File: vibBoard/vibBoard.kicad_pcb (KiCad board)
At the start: 2 copper layers, 32.4 x 45.1 mm, 39 parts, among them J1 CAN Bus Connector, J2 Programming Header, J3 Micro_SD_Card, U1 SPX3819M5-L-3-3, U2 INA180, U3 AIS3624DQTR, U4 PIC18F26K83, U5 MCP2562, Y1 12MHz Crystal

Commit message: updated date
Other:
- board text added: "Vibration Board V1 Ishman Mann 2024-02-01"
- board text removed: "Vibration Board V1 Ishman Mann 2024-01-13"
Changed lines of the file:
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@@
     (effects (font (size 1.5 1.5) (thickness 0.3) bold) (justify left bottom))
   )
-  (gr_text "Vibration Board V1\nIshman Mann\n2024-01-13" (at 125.984 110.236) (layer "F.SilkS")
+  (gr_text "Vibration Board V1\nIshman Mann\n2024-02-01" (at 125.984 110.236) (layer "F.SilkS")
     (effects (font (size 0.8001 0.635) (thickness 0.127) bold))
   )

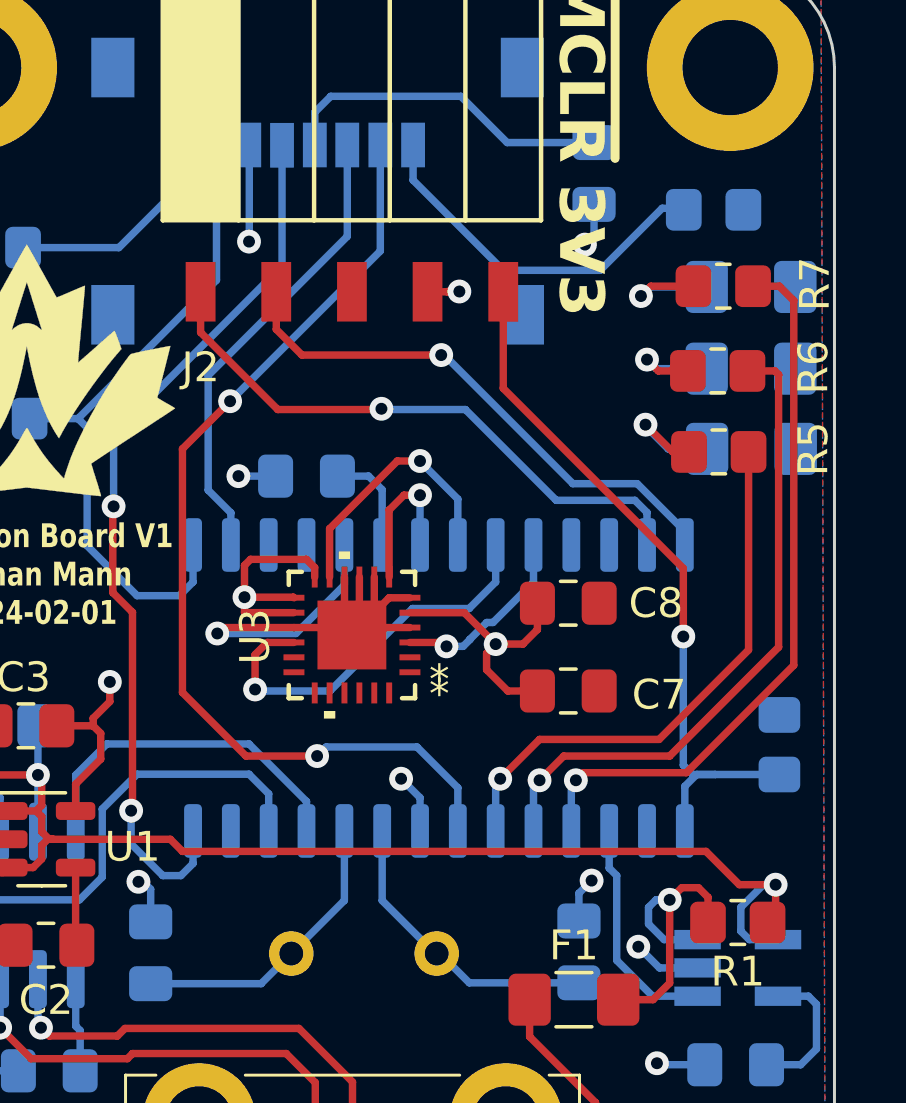
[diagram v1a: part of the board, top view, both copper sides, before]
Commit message: switched diode side and added more continuity to planes
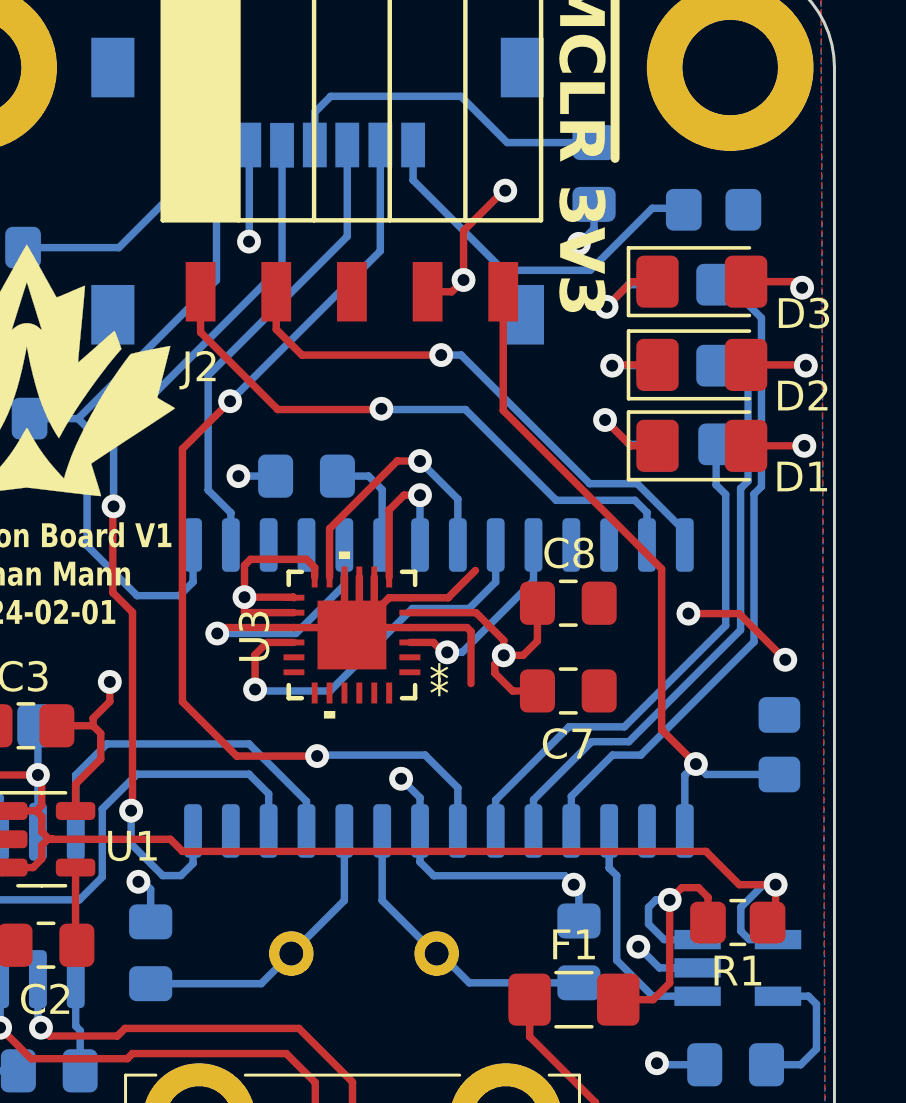
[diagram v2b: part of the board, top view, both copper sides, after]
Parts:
- D1, D2, D3: moved to F.Cu
- R5, R6, R7: moved to B.Cu
- moved D1 1.67 mm to (148.4, 105.9)
- moved D3 1.66 mm to (148.4, 100.4)
- moved D2 1.66 mm to (148.4, 103.2)
- moved R7 1.31 mm to (147.8, 100.5)
- moved R6 1.13 mm to (147.8, 103.2)
- moved R5 1.12 mm to (147.9, 105.9)
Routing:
- net +3.3V: track 47.8 -> 62.1 mm, vias 4 -> 10
- net GND: track 52.1 -> 65.3 mm
- net Net-(U4-RA2): track 24.7 -> 22.0 mm, vias 1 -> 0
- net Net-(U4-RA3): track 22.0 -> 19.7 mm, vias 1 -> 0
- net Net-(U4-RA4): track 18.7 -> 17.4 mm, vias 1 -> 0
- net Net-(D2-K): track 3.75 -> 2.95 mm
- net /~{MCLR}: track 24.5 -> 23.9 mm

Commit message: touch up
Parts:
- moved Y1 0.45 mm to (139.5, 123.4)
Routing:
- net /CANL: track 14.4 -> 13.5 mm
- net /CANH: track 19.1 -> 18.6 mm
- net GND: vias 13 -> 32
- added copper zone on B.Cu, net GND
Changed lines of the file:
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@@
   )
   (footprint "Crystal:Crystal_HC49-4H_Vertical" (layer "B.Cu")
-    (at 139.4968 122.962 180)
+    (at 139.5468 123.412 180)
     (descr "Crystal THT HC-49-4H http://5hertz.com/pdfs/04404_D.pdf")
     (tags "THT crystalHC-49-4H")
@@
   (segment (start 132.33 112.018) (end 134.7057 112.018) (width 0.25) (layer "F.Cu") (net 2))
   (segment (start 136.902 112.018) (end 136.652 112.268) (width 0.25) (layer "F.Cu") (net 2))
+  (via (at 140.65 122.05) (size 0.8) (drill 0.4) (layers "F.Cu" "B.Cu") (free) (net 2))
+  (via (at 139.25 125.25) (size 0.8) (drill 0.4) (layers "F.Cu" "B.Cu") (free) (net 2))
   (via (at 129.484901 120.552699) (size 0.8) (drill 0.4) (layers "F.Cu" "B.Cu") (net 2))
   (via (at 132.1308 112.2172) (size 0.8) (drill 0.4) (layers "F.Cu" "B.Cu") (net 2))
   (via (at 133.1976 99.06) (size 0.8) (drill 0.4) (layers "F.Cu" "B.Cu") (net 2))
   (via (at 123.2662 126.9238) (size 0.8) (drill 0.4) (layers "F.Cu" "B.Cu") (net 2))
+  (via (at 132.55 121.3) (size 0.8) (drill 0.4) (layers "F.Cu" "B.Cu") (free) (net 2))
+  (via (at 138.25 124.6) (size 0.8) (drill 0.4) (layers "F.Cu" "B.Cu") (free) (net 2))
+  (via (at 133.5 122.05) (size 0.8) (drill 0.4) (layers "F.Cu" "B.Cu") (free) (net 2))
+  (via (at 133.8 125.0255) (size 0.8) (drill 0.4) (layers "F.Cu" "B.Cu") (free) (net 2))
+  (via (at 140.4 125) (size 0.8) (drill 0.4) (layers "F.Cu" "B.Cu") (free) (net 2))
+  (via (at 135.95 124.6) (size 0.8) (drill 0.4) (layers "F.Cu" "B.Cu") (free) (net 2))
   (via (at 121.666 125.7554) (size 0.8) (drill 0.4) (layers "F.Cu" "B.Cu") (net 2))
+  (via (at 134.5 121.6) (size 0.8) (drill 0.4) (layers "F.Cu" "B.Cu") (free) (net 2))
   (via (at 146.2665 122.7328) (size 0.8) (drill 0.4) (layers "F.Cu" "B.Cu") (net 2))
+  (via (at 132.85 122.85) (size 0.8) (drill 0.4) (layers "F.Cu" "B.Cu") (free) (net 2))
+  (via (at 141.6 121.25) (size 0.8) (drill 0.4) (layers "F.Cu" "B.Cu") (free) (net 2))
+  (via (at 137.85 123.6) (size 0.8) (drill 0.4) (layers "F.Cu" "B.Cu") (free) (net 2))
+  (via (at 139.5 121.6) (size 0.8) (drill 0.4) (layers "F.Cu" "B.Cu") (free) (net 2))
   (via (at 146.8921 126.6444) (size 0.8) (drill 0.4) (layers "F.Cu" "B.Cu") (net 2))
   (via (at 144.272 99.1362) (size 0.8) (drill 0.4) (layers "F.Cu" "B.Cu") (net 2))
+  (via (at 141.25 125) (size 0.8) (drill 0.4) (layers "F.Cu" "B.Cu") (free) (net 2))
+  (via (at 135.05 125.2) (size 0.8) (drill 0.4) (layers "F.Cu" "B.Cu") (free) (net 2))
   (via (at 132.842 106.934) (size 0.8) (drill 0.4) (layers "F.Cu" "B.Cu") (net 2))
   (via (at 138.303 117.094) (size 0.8) (drill 0.4) (layers "F.Cu" "B.Cu") (net 2))
+  (via (at 132.95 125.0255) (size 0.8) (drill 0.4) (layers "F.Cu" "B.Cu") (free) (net 2))
   (via (at 122.555 116.205) (size 0.8) (drill 0.4) (layers "F.Cu" "B.Cu") (net 2))
+  (via (at 136.35 123.6) (size 0.8) (drill 0.4) (layers "F.Cu" "B.Cu") (free) (net 2))
+  (via (at 137.1 122.6) (size 0.8) (drill 0.4) (layers "F.Cu" "B.Cu") (free) (net 2))
   (via (at 135.6868 131.4704) (size 0.8) (drill 0.4) (layers "F.Cu" "B.Cu") (net 2))
   (via (at 144.1 120.65) (size 0.8) (drill 0.4) (layers "F.Cu" "B.Cu") (net 2))
+  (via (at 141.3 122.85) (size 0.8) (drill 0.4) (layers "F.Cu" "B.Cu") (free) (net 2))
   (segment (start 122.555 116.713) (end 123.0376 117.1956) (width 0.25) (layer "B.Cu") (net 2))
   (segment (start 144.78 98.6282) (end 144.272 99.1362) (width 0.25) (layer "B.Cu") (net 2))
@@
   (segment (start 152.2476 124.6632) (end 152.2476 126.1657) (width 0.25) (layer "B.Cu") (net 4))
   (segment (start 137.2108 106.934) (end 137.668 107.3912) (width 0.25) (layer "B.Cu") (net 4))
-  (segment (start 137.668 121.1834) (end 139.4466 122.962) (width 0.25) (layer "B.Cu") (net 5))
-  (segment (start 137.668 118.846) (end 137.668 121.1834) (width 0.25) (layer "B.Cu") (net 5))
-  (segment (start 144.272 123.9442) (end 140.5922 123.9442) (width 0.25) (layer "B.Cu") (net 5))
+  (segment (start 144.272 123.9442) (end 140.079 123.9442) (width 0.25) (layer "B.Cu") (net 5))
+  (segment (start 140.079 123.9442) (end 139.5468 123.412) (width 0.25) (layer "B.Cu") (net 5))
+  (segment (start 137.668 121.5332) (end 139.5468 123.412) (width 0.25) (layer "B.Cu") (net 5))
   (segment (start 139.3196 122.962) (end 139.61 122.962) (width 0.25) (layer "B.Cu") (net 5))
   (segment (start 139.4466 122.962) (end 139.4968 122.962) (width 0.25) (layer "B.Cu") (net 5))
-  (segment (start 140.5922 123.9442) (end 139.61 122.962) (width 0.25) (layer "B.Cu") (net 5))
+  (segment (start 137.668 118.846) (end 137.668 121.5332) (width 0.25) (layer "B.Cu") (net 5))
+  (segment (start 136.398 118.846) (end 136.398 121.6808) (width 0.25) (layer "B.Cu") (net 6))
+  (segment (start 136.398 121.6808) (end 134.6668 123.412) (width 0.25) (layer "B.Cu") (net 6))
   (segment (start 134.7464 122.962) (end 134.73 122.962) (width 0.25) (layer "B.Cu") (net 6))
-  (segment (start 136.398 118.846) (end 136.398 121.1808) (width 0.25) (layer "B.Cu") (net 6))
-  (segment (start 129.8956 123.9735) (end 133.6053 123.9735) (width 0.25) (layer "B.Cu") (net 6))
-  (segment (start 133.6053 123.9735) (end 134.6168 122.962) (width 0.25) (layer "B.Cu") (net 6))
-  (segment (start 136.398 121.1808) (end 134.6168 122.962) (width 0.25) (layer "B.Cu") (net 6))
+  (segment (start 129.8956 123.9735) (end 134.1053 123.9735) (width 0.25) (layer "B.Cu") (net 6))
+  (segment (start 134.1053 123.9735) (end 134.6668 123.412) (width 0.25) (layer "B.Cu") (net 6))
   (segment (start 145.15 105.05) (end 146.018 105.918) (width 0.25) (layer "F.Cu") (net 7))
   (segment (start 146.018 105.918) (end 146.9104 105.918) (width 0.25) (layer "F.Cu") (net 7))
@@
   (segment (start 147.132 122.494) (end 148.256 122.494) (width 0.25) (layer "B.Cu") (net 11))
   (segment (start 146.8628 121.158) (end 146.6088 121.412) (width 0.25) (layer "B.Cu") (net 11))
-  (segment (start 126.492 125.73) (end 128.778 125.73) (width 0.25) (layer "F.Cu") (net 13))
-  (segment (start 128.778 125.73) (end 129.032 125.476) (width 0.25) (layer "F.Cu") (net 13))
-  (segment (start 126.2126 125.4506) (end 126.492 125.73) (width 0.25) (layer "F.Cu") (net 13))
-  (segment (start 136.672 127.274) (end 136.672 128.544) (width 0.25) (layer "F.Cu") (net 13))
-  (segment (start 129.032 125.476) (end 134.874 125.476) (width 0.25) (layer "F.Cu") (net 13))
-  (segment (start 134.874 125.476) (end 136.672 127.274) (width 0.25) (layer "F.Cu") (net 13))
+  (segment (start 126.2126 125.4506) (end 126.712 125.95) (width 0.25) (layer "F.Cu") (net 13))
+  (segment (start 130.313604 125.8) (end 133.928 125.8) (width 0.25) (layer "F.Cu") (net 13))
+  (segment (start 133.928 125.8) (end 136.672 128.544) (width 0.25) (layer "F.Cu") (net 13))
+  (segment (start 130.163604 125.95) (end 130.313604 125.8) (width 0.25) (layer "F.Cu") (net 13))
+  (segment (start 126.712 125.95) (end 130.163604 125.95) (width 0.25) (layer "F.Cu") (net 13))
   (via (at 126.2126 125.4506) (size 0.8) (drill 0.4) (layers "F.Cu" "B.Cu") (net 13))
   (segment (start 126.2126 125.4506) (end 126.111 125.349) (width 0.25) (layer "B.Cu") (net 13))
   (segment (start 126.111 125.349) (end 126.111 123.822) (width 0.25) (layer "B.Cu") (net 13))
-  (segment (start 135.422 127.294) (end 135.422 128.544) (width 0.25) (layer "F.Cu") (net 14))
-  (segment (start 129.113 126.492) (end 129.286 126.319) (width 0.25) (layer "F.Cu") (net 14))
-  (segment (start 134.447 126.319) (end 135.422 127.294) (width 0.25) (layer "F.Cu") (net 14))
+  (segment (start 130.258 126.492) (end 130.5 126.25) (width 0.25) (layer "F.Cu") (net 14))
+  (segment (start 133.4 126.25) (end 135.422 128.272) (width 0.25) (layer "F.Cu") (net 14))
+  (segment (start 130.5 126.25) (end 133.4 126.25) (width 0.25) (layer "F.Cu") (net 14))
+  (segment (start 135.422 128.272) (end 135.422 128.544) (width 0.25) (layer "F.Cu") (net 14))
   (segment (start 124.841 125.4506) (end 125.8824 126.492) (width 0.25) (layer "F.Cu") (net 14))
-  (segment (start 129.286 126.319) (end 134.447 126.319) (width 0.25) (layer "F.Cu") (net 14))
-  (segment (start 125.8824 126.492) (end 129.113 126.492) (width 0.25) (layer "F.Cu") (net 14))
+  (segment (start 125.8824 126.492) (end 130.258 126.492) (width 0.25) (layer "F.Cu") (net 14))
   (via (at 124.841 125.4506) (size 0.8) (drill 0.4) (layers "F.Cu" "B.Cu") (net 14))
   (segment (start 135.2604 128.544) (end 133.7564 130.048) (width 0.25) (layer "B.Cu") (net 14))
@@
     (polygon
       (pts
-        (xy 120.9548 90.0684)
-        (xy 120.8786 134.3152)
-        (xy 152.5524 134.3152)
-        (xy 152.4 90.1446)
+        (xy 120.15 89.25)
+        (xy 119.8 135.7)
+        (xy 153.6 135.75)
+        (xy 153.4 89.3)
       )
     )
@@
     (polygon
       (pts
-        (xy 120.9294 90.0684)
-        (xy 120.8786 134.3152)
-        (xy 152.5524 134.366)
-        (xy 152.4 90.1446)
+        (xy 120.1 89.3)
+        (xy 119.8 135.7)
+        (xy 153.6 135.75)
+        (xy 153.35 89.3)
       )
     )
+  )
+  (zone (net 2) (net_name "GND") (layer "B.Cu") (hatch edge 0.5)
+    (priority 5)
+    (connect_pads (clearance 0.5))
+    (min_thickness 0.25) (filled_areas_thickness no)
+    (fill yes (thermal_gap 0.5) (thermal_bridge_width 0.5))
+    (polygon
+      (pts
+        (xy 132.1 120.8)
+        (xy 132.1 125.8)
+        (xy 142.05 125.75)
+        (xy 142.05 120.8)
+      )
+    )

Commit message: layout
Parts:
- added J4: THMS Connector, Connector_JST:JST_PH_S2B-PH-K_1x02_P2.00mm_Horizontal, F.Cu at (165.4, 126.0)
- added J5: PT 1 Connector, Connector_JST:JST_PH_S3B-PH-K_1x03_P2.00mm_Horizontal, F.Cu at (165.4, 118.9)
- added J6: PT 2 Connector, Connector_JST:JST_PH_S3B-PH-K_1x03_P2.00mm_Horizontal, F.Cu at (165.4, 109.5)
- added R10: 5kR, Resistor_SMD:R_0805_2012Metric_Pad1.20x1.40mm_HandSolder, B.Cu at (160.5, 113.5)
- added R11: 10kR, Resistor_SMD:R_0805_2012Metric_Pad1.20x1.40mm_HandSolder, B.Cu at (160.5, 108.4)
- added R12: 5kR, Resistor_SMD:R_0805_2012Metric_Pad1.20x1.40mm_HandSolder, B.Cu at (156.5, 103.9)
- added R13: 10kR, Resistor_SMD:R_0805_2012Metric_Pad1.20x1.40mm_HandSolder, B.Cu at (156.5, 99.1)
- added R9: 10kR, Resistor_SMD:R_0805_2012Metric_Pad1.20x1.40mm_HandSolder, B.Cu at (147.3, 127.8)
- C1, C2, C3, F1, R1, U1: moved to B.Cu
- C10, C12, C5, C6, C9, J3, TP1, U5, Y1: moved to F.Cu
- moved C1 38.8 mm to (160.8, 125.0), turned to 90 degrees
- moved C12 33.4 mm to (158.2, 118.4), turned to 180 degrees
- moved U5 32.2 mm to (157.6, 123.8)
- moved U1 32.0 mm to (157.5, 125.6), turned to 90 degrees
- moved C10 31.6 mm to (158.0, 129.5), turned to 180 degrees
- moved C2 27.9 mm to (154.2, 125.5), turned to -90 degrees
- moved D1 27.3 mm to (133.4, 128.7), turned to 180 degrees
- moved R5 27.1 mm to (133.3, 128.7)
- moved D2 26.9 mm to (133.4, 125.5), turned to 180 degrees
- moved C3 26.6 mm to (150.9, 124.0), turned to 90 degrees
- moved R6 26.6 mm to (133.3, 125.6), turned to 180 degrees
- moved D3 26.6 mm to (133.4, 122.3), turned to 180 degrees
- moved R7 26.1 mm to (133.3, 122.3), turned to 180 degrees
- moved C9 25.7 mm to (132.6, 119.4), turned to 0 degrees
- moved G*** 24.6 mm to (101.1, 102.6)
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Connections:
- net /PIC_CANRX renamed /CANRX
- net /PIC_CANTX renamed /CANTX
- net /PIC_SCK1 renamed /MICRO_SD_SCK
- net /PIC_SDI1 renamed /MICRO_SD_SDI
- net /PIC_SDO1 renamed /MICRO_SD_SDO
- U4 pad 2: unconnected-(U4-RA0-Pad2) -> /THMS_SENSE
- U4 pad 25: unconnected-(U4-RB4-Pad25) -> /PT_2_SENSE
- U4 pad 26: unconnected-(U4-RB5-Pad26) -> /PT_1_SENSE
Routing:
- net GND: track 65.3 -> 0.00 mm, vias 32 -> 0
- net +3.3V: track 62.1 -> 0.00 mm, vias 10 -> 0
- net +5V: track 45.2 -> 0.00 mm, vias 2 -> 0
- net /MICRO_SD_CS: track 33.4 -> 0.00 mm, vias 2 -> 0
- net /MICRO_SD_SCK: track 29.9 -> 0.00 mm, vias 2 -> 0
- net /~{MCLR}: track 23.9 -> 0.00 mm, vias 1 -> 0
- net /MICRO_SD_SDI: track 23.2 -> 0.00 mm
- net Net-(U4-RA2): track 22.0 -> 0.00 mm
- net /ICSPCLK: track 20.0 -> 0.00 mm, vias 1 -> 0
- net Net-(U4-RA3): track 19.7 -> 0.00 mm
- net /CANH: track 18.6 -> 0.00 mm, vias 1 -> 0
- net /ICSPDAT: track 18.2 -> 0.00 mm, vias 1 -> 0
- net Net-(U4-RA4): track 17.4 -> 0.00 mm
- net /CANRX: track 16.8 -> 0.00 mm
- net Net-(J1-Pin_5): track 16.6 -> 0.00 mm
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- removed copper zone on B.Cu, net +3.3V
- removed copper zone on B.Cu, net GND
- removed copper zone on F.Cu, net GND
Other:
- board size 32.4 x 45.1 mm -> 45.7 x 45.7 mm
- board text added: "Vibration Board V2 Ishman Mann 2024-03-14"
- board text removed: "Vibration Board V1 Ishman Mann 2024-02-01"

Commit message: routing begins
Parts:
- C5, C6: moved to B.Cu
- moved R9 19.2 mm to (162.6, 116.1), turned to 90 degrees
- moved C3 11.6 mm to (162.3, 122.2)
- moved TP1 11.5 mm to (137.4, 137.2)
- moved R10 9.92 mm to (170.2, 115.8)
- moved R11 9.68 mm to (170.2, 109.2)
- moved R3 8.90 mm to (132.1, 109.5)
- moved R12 7.74 mm to (163.3, 107.4), turned to 180 degrees
- moved R13 5.30 mm to (159.5, 103.4)
- moved R5 4.99 mm to (136.9, 125.2), turned to -90 degrees
- moved D1 4.94 mm to (136.9, 125.2), turned to -90 degrees
- moved D3 4.19 mm to (130.4, 125.3), turned to -90 degrees
- moved R7 4.14 mm to (130.5, 125.2), turned to -90 degrees
- moved C1 3.47 mm to (161.8, 128.3), turned to 0 degrees
- moved C12 3.06 mm to (160.3, 116.1)
- moved C11 2.62 mm to (147.1, 104.6), turned to 0 degrees
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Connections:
- U4 pad 25: /PT_2_SENSE -> /PT_1_SENSE
- U4 pad 26: /PT_1_SENSE -> /PT_2_SENSE
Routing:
- net Net-(U4-RA2): track 0.00 -> 36.0 mm
- net Net-(U4-RA3): track 0.00 -> 32.4 mm
- net /THMS_SENSE: track 0.00 -> 30.0 mm
- net /CANRX: track 0.00 -> 29.7 mm, vias 0 -> 1
- net Net-(U4-RA4): track 0.00 -> 28.7 mm
- net /PT_1_SENSE: track 0.00 -> 24.6 mm
- net /CURR_SENSE: track 0.00 -> 21.2 mm
- net /CANH: track 0.00 -> 20.9 mm
- net /CANTX: track 0.00 -> 20.9 mm, vias 0 -> 1
- net /~{MCLR}: track 0.00 -> 19.0 mm, vias 0 -> 1
- net /CANL: track 0.00 -> 18.5 mm
- net /MICRO_SD_CS: track 0.00 -> 17.9 mm, vias 0 -> 1
- net /MICRO_SD_SCK: track 0.00 -> 17.3 mm, vias 0 -> 1
- net /PT_2_SENSE: track 0.00 -> 15.8 mm
- net /MICRO_SD_SDI: track 0.00 -> 14.8 mm, vias 0 -> 1
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- added copper zone on B.Cu, net +5V
